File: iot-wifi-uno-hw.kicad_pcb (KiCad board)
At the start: 2 copper layers, 68.6 x 53.3 mm, 83 parts, among them CON1 BARREL_JACK, P1 CONN_01X08, P2 CONN_01X08, P3 CONN_01X06, P4 CONN_01X10, P5 CONN_01X04, Q1 Q_NPN_BEC, Q2 Q_NPN_BEC, U1 usb_mini_b, U2 MCP16311-MNY, U3 CH340G, U4 ESP-12E, U5 MCP6001R, U6 BD00GA5WEFJ, U7 IRLM6402, X1 CRYSTAL_ABM3C

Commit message: Fix Via & update assets
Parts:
- removed REF** (x12): gnd_via, ESP8266:gnd_via
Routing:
- net GND: track 300.3 -> 313.6 mm, vias 7 -> 10
- net GPIO14: track 56.7 -> 50.4 mm
- net GPIO5: track 133.7 -> 128.7 mm
- net GPIO4: track 131.9 -> 134.6 mm
- net MOSI: track 40.4 -> 38.5 mm
- net REST: track 110.7 -> 112.5 mm
- net MISO: track 30.9 -> 31.9 mm
- net GPIO0: track 83.7 -> 84.7 mm
- net SCLK: track 39.8 -> 38.9 mm
- net GPIO10: track 38.2 -> 37.5 mm
- net Net-(GPIO1-Pad1): track 81.3 -> 81.9 mm
- net GPIO13: track 46.1 -> 46.7 mm
- net GPIO16: track 58.2 -> 58.8 mm
- net GPIO15: track 47.7 -> 47.2 mm
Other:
- rule trace_min: 0.2 -> 0.254

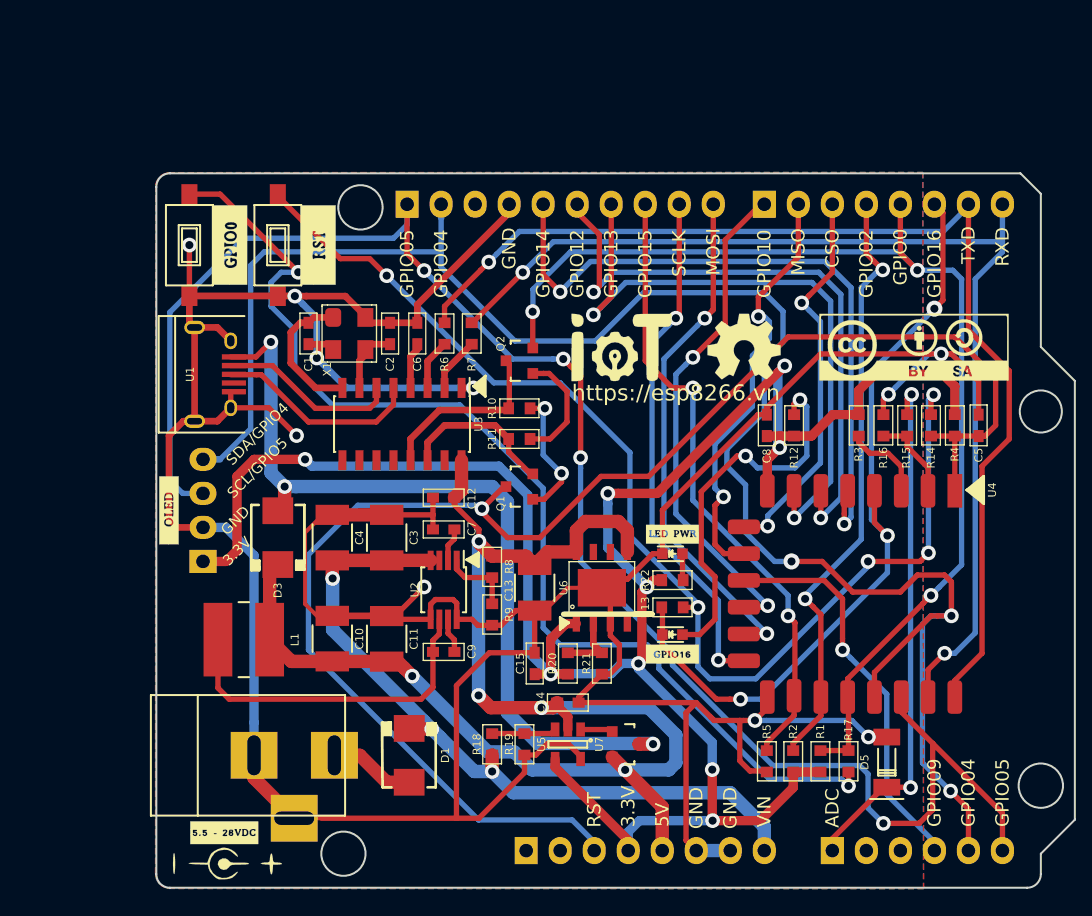
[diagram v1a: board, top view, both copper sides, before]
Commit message: change IC CH340G to PL2303HXD
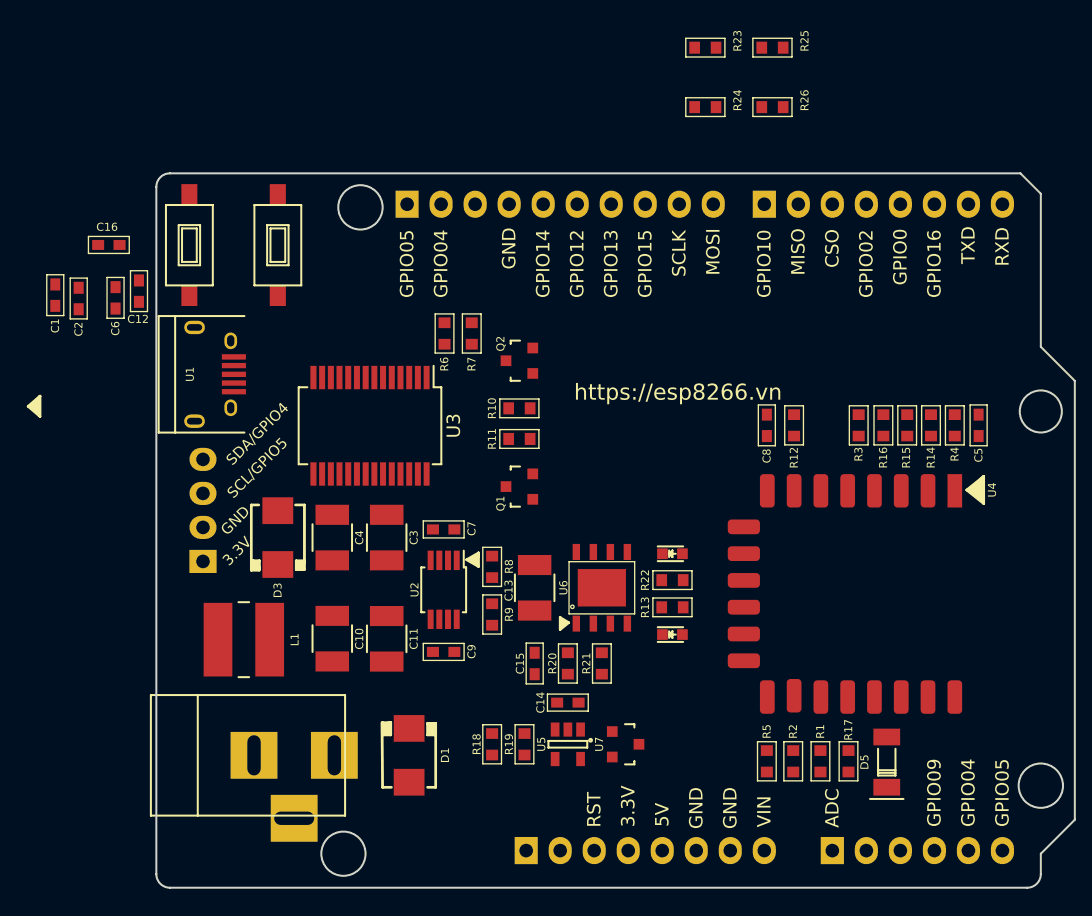
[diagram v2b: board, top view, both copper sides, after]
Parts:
- removed G***: LOGO, ESP8266:logo-jack-5528
- removed G***: LOGO, ESP8266:logo_openhardware_5x5mm
- removed G***: LOGO, ESP8266:logo-jack_7.4x3
- removed G***: LOGO, ESP8266:logo_cc-bby-sa_14.1x5mm
- removed G***: LOGO, ESP8266:logo-iotmakervn_7.5x5
- removed G***: LOGO, ESP8266:LEDPWR
- removed G***: LOGO, ESP8266:GPIO16
- removed G***: LOGO, ESP8266:RST
- removed G***: LOGO, ESP8266:GPIO0
- removed G***: LOGO, ESP8266:logo-iotmakervn_7
- removed X1: CRYSTAL_ABM3C, ESP8266:Crystal_SMD_3225_4Pads
- added C16: 10uF, ESP8266:C_0603, F.Cu at (106.0, 64.0)
- added R23: 4k7, ESP8266:R_0603, F.Cu at (150.5, 49.3)
- added R24: 27R, ESP8266:R_0603, F.Cu at (150.5, 53.7)
- added R25: 27R, ESP8266:R_0603, F.Cu at (155.5, 49.3)
- added R26: 1k5, ESP8266:R_0603, F.Cu at (155.5, 53.7)
- C1: value 22pF -> 0.1uF
- C12, C6: value 100nF -> 0.1uF
- C2: value 22pF -> 10uF
- R13: value 0R -> 0R-NC
- U3: value CH340G -> pl2303; footprint Housings_SOIC:SOIC-16_3.9x9.9mm_Pitch1.27mm -> Housings_SSOP:SSOP-28_5.3x10.2mm_Pitch0.65mm
- moved C12 27.5 mm to (108.2, 67.5), turned to 90 degrees
- moved C2 23.4 mm to (103.8, 68.0)
- moved C6 22.7 mm to (106.5, 68.0)
- moved C1 19.1 mm to (102.0, 67.8)
- moved U3 2.39 mm to (125.5, 77.5)
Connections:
- C1 pad 1: XO -> +3V3
- C12 pad 1: +5V -> GND
- C12 pad 2: GND -> +3V3
- C2 pad 1: XI -> VCC
- C6 pad 1: Net-(C6-Pad1) -> GND
- C6 pad 2: GND -> +5V
- Q1 pad 2: Net-(Q1-Pad2) -> RTS-N
- Q2 pad 3: Net-(Q2-Pad3) -> DTR-N
- R10 pad 1: Net-(Q2-Pad3) -> DTR-N
- R11 pad 1: Net-(Q1-Pad2) -> RTS-N
- R6 pad 2: Net-(R6-Pad2) -> RXD-2303
- R7 pad 2: Net-(R7-Pad2) -> TXD-2303
- U3 pad 1: GND -> TXD-2303
- U3 pad 10: (no net) -> DCD-N
- U3 pad 13: Net-(Q2-Pad3) -> (no net)
- U3 pad 14: Net-(Q1-Pad2) -> (no net)
- U3 pad 15: (no net) -> Net-(R24-Pad1)
- U3 pad 16: +5V -> Net-(R25-Pad1)
- U3 pad 2: Net-(R7-Pad2) -> DTR-N
- U3 pad 3: Net-(R6-Pad2) -> RTS-N
- U3 pad 4: Net-(C6-Pad1) -> +3V3
- U3 pad 5: D+ -> RXD-2303
- U3 pad 6: D- -> (no net)
- U3 pad 7: XI -> GND
- U3 pad 8: XO -> (no net)
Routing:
- net GND: track 313.6 -> 0.00 mm, vias 10 -> 0
- net +3V3: track 165.3 -> 0.00 mm, vias 9 -> 0
- net GPIO4: track 134.6 -> 0.00 mm, vias 3 -> 0
- net GPIO5: track 128.7 -> 0.00 mm, vias 4 -> 0
- net REST: track 112.5 -> 0.00 mm, vias 1 -> 0
- net +5V: track 105.5 -> 0.00 mm, vias 5 -> 0
- net Net-(R13-Pad2): track 88.8 -> 0.00 mm, vias 5 -> 0
- net GPIO0: track 84.7 -> 0.00 mm, vias 3 -> 0
- net TXD: track 82.6 -> 0.00 mm, vias 1 -> 0
- net Net-(GPIO1-Pad1): track 81.9 -> 0.00 mm, vias 2 -> 0
- net RXD: track 81.0 -> 0.00 mm, vias 2 -> 0
- net VCC: track 62.4 -> 0.00 mm, vias 3 -> 0
- net GPIO16: track 58.8 -> 0.00 mm, vias 3 -> 0
- net Vin: track 56.2 -> 0.00 mm, vias 3 -> 0
- net GPIO14: track 50.4 -> 0.00 mm, vias 2 -> 0
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- removed copper zone on B.Cu, net GND
- removed copper zone on F.Cu, net GND

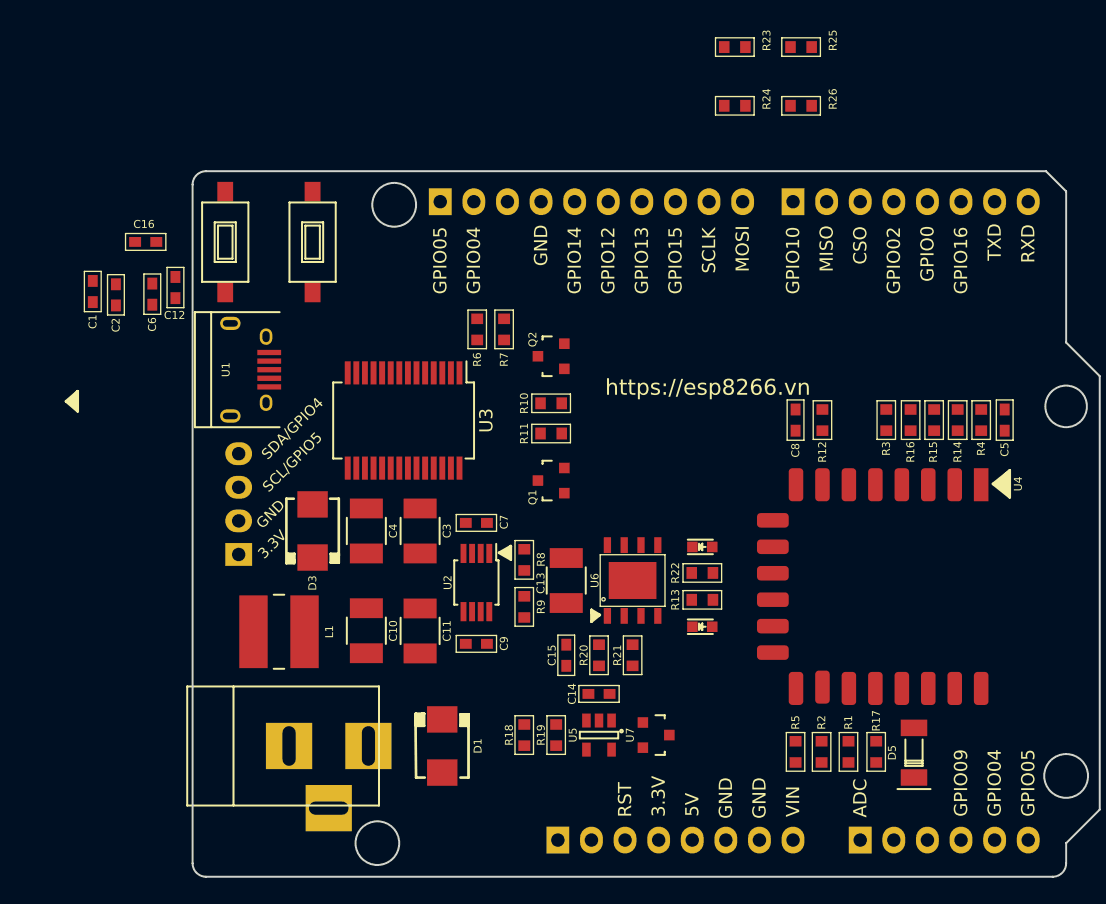
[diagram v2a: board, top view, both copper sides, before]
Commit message: setup new PCB
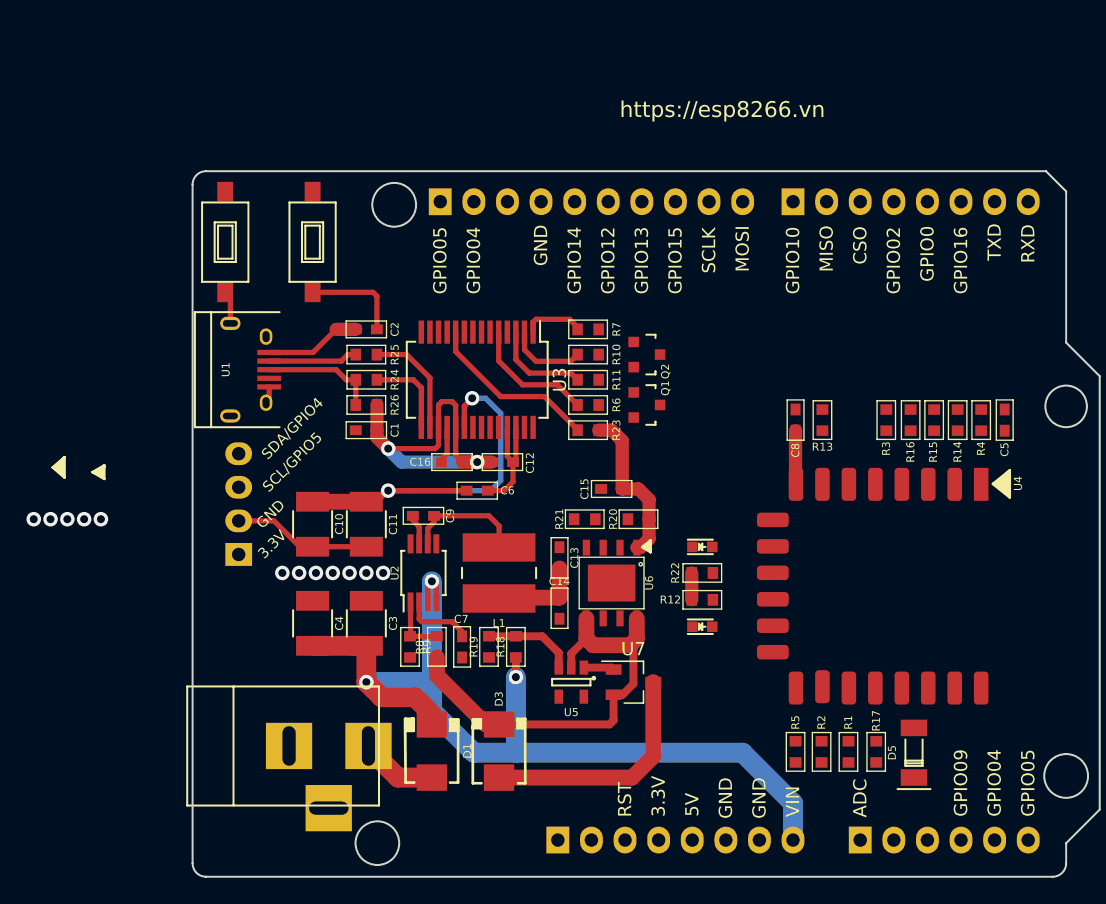
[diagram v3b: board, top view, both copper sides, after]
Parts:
- C13: footprint ESP8266:C_1210 -> ESP8266:C_0603
- U7: footprint TO_SOT_Packages_SMD:SOT-23 -> TO_SOT_Packages_SMD:SOT-23_Handsoldering
- moved R25 40.3 mm to (122.7, 72.5), turned to 180 degrees
- moved R26 39.9 mm to (122.7, 76.3)
- moved R24 34.7 mm to (122.7, 74.4), turned to 180 degrees
- moved R23 31.0 mm to (139.4, 78.2), turned to 180 degrees
- moved C6 28.7 mm to (131.1, 82.8), turned to 180 degrees
- moved C16 28.5 mm to (129.2, 80.6)
- moved C12 28.0 mm to (133.0, 80.6), turned to 180 degrees
- moved C1 23.2 mm to (122.7, 78.2), turned to 180 degrees
- moved D3 21.8 mm to (132.7, 102.5), turned to 270 degrees
- moved C2 19.1 mm to (122.7, 70.6), turned to 0 degrees
- moved L1 17.2 mm to (132.7, 89.0), turned to 270 degrees
- moved R12 16.3 mm to (148.1, 91.1), turned to 0 degrees
- moved R13 16.3 mm to (157.2, 77.5), turned to 90 degrees
- moved C15 13.0 mm to (141.2, 82.7), turned to 180 degrees
- moved R21 10.9 mm to (139.2, 85.0), turned to 180 degrees
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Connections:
- R26 pad 1: D- -> D+
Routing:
- net Vin: track 0.00 -> 71.9 mm, vias 0 -> 3
- net +5V: track 0.00 -> 70.9 mm, vias 0 -> 2
- net +3V3: track 0.00 -> 45.1 mm, vias 0 -> 2
- net GND: track 0.00 -> 33.7 mm
- net VCC: track 0.00 -> 25.2 mm
- net DCD-N: track 0.00 -> 13.2 mm
- net RXD-2303: track 0.00 -> 9.51 mm
- net Net-(C9-Pad2): track 0.00 -> 9.17 mm
- net D+: track 0.00 -> 8.77 mm
- net Net-(R25-Pad1): track 0.00 -> 8.48 mm
- net RTS-N: track 0.00 -> 7.37 mm
- net Net-(R18-Pad1): track 0.00 -> 6.91 mm
- net D-: track 0.00 -> 6.75 mm
- net Net-(R24-Pad1): track 0.00 -> 6.60 mm
- net DTR-N: track 0.00 -> 5.91 mm
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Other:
- net class Default: clearance 0.254 -> 0.2; trace_width 0.4 -> 0.6
- rule trace_clearance: 0.254 -> 0.2

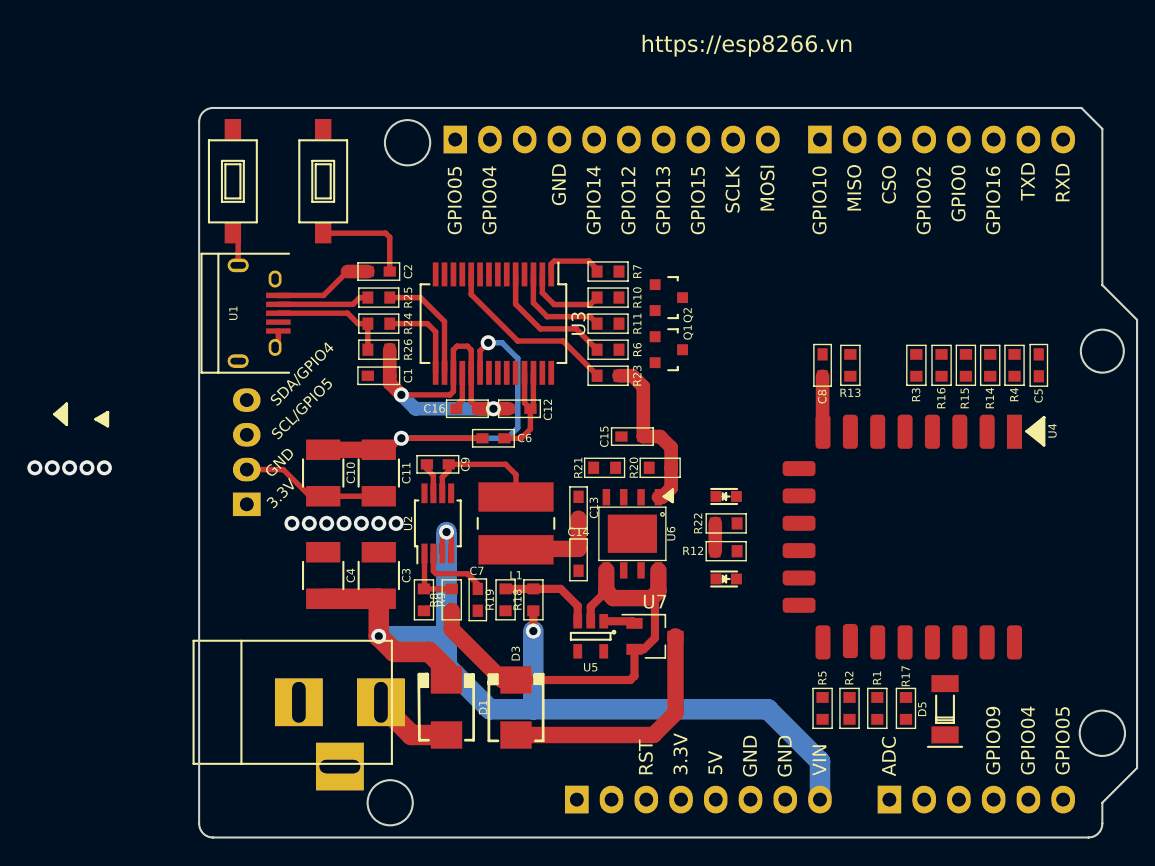
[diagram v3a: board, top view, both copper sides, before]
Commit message: fix error button & modify CH340G 5V to 3.3V, Update PCB
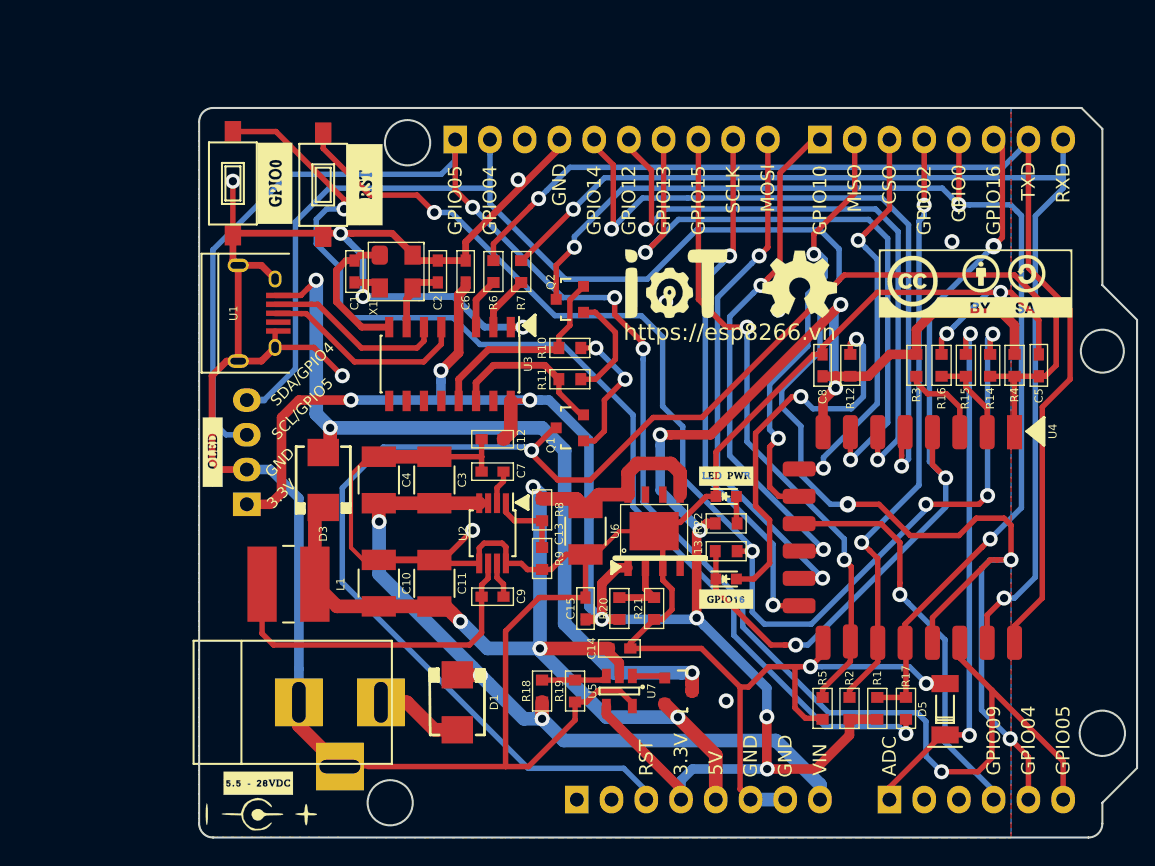
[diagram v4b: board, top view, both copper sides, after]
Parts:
- removed C16: 10uF, ESP8266:C_0603
- removed GPIO1: GPIO0, ESP8266:Tact_Switch_TS6X3.6
- removed R23: 4k7, ESP8266:R_0603
- removed R24, R25: 27R, ESP8266:R_0603
- removed R26: 1k5, ESP8266:R_0603
- removed RST1: REST, ESP8266:Tact_Switch_TS6X3.6
- added G***: LOGO, ESP8266:RST, F.Cu at (121.7, 64.3)
- added G***: LOGO, ESP8266:logo_cc-bby-sa_14.1x5mm, F.Cu at (166.3, 71.5)
- added G***: LOGO, ESP8266:GPIO0, F.Cu at (115.1, 64.2)
- added G***: LOGO, ESP8266:logo-iotmakervn_7, F.Cu at (110.5, 83.8)
- added G***: LOGO, ESP8266:logo-jack-5528, F.Cu at (113.9, 108.0)
- added G***: LOGO, ESP8266:logo-jack_7.4x3, F.Cu at (113.9, 110.2)
- added G***: LOGO, ESP8266:LEDPWR, F.Cu at (148.1, 85.6)
- added G***: LOGO, ESP8266:GPIO16, F.Cu at (148.1, 94.6)
- added G***: LOGO, ESP8266:logo-iotmakervn_7.5x5, F.Cu at (144.4, 71.5)
- added G***: LOGO, ESP8266:logo_openhardware_5x5mm, F.Cu at (153.4, 71.6)
- added SW1: RST, ESP8266:Tact_Switch_TS6X3.6, F.Cu at (118.6, 64.3)
- added SW2: GPIO0, ESP8266:Tact_Switch_TS6X3.6, F.Cu at (112.0, 64.2)
- added X1: CRYSTAL_ABM3C, ESP8266:Crystal_SMD_3225_4Pads, F.Cu at (124.0, 70.6)
- C1: value 0.1uF -> 22pF
- C12, C6: value 0.1uF -> 100nF
- C13: footprint ESP8266:C_0603 -> ESP8266:C_1210
- C2: value 10uF -> 22pF
- R13: value 0R-NC -> 0R
- U3: value pl2303 -> CH340G; footprint Housings_SSOP:SSOP-28_5.3x10.2mm_Pitch0.65mm -> Housings_SOIC:SOIC-16_3.9x9.9mm_Pitch1.27mm
- U7: footprint TO_SOT_Packages_SMD:SOT-23_Handsoldering -> TO_SOT_Packages_SMD:SOT-23
- moved D3 21.8 mm to (118.6, 85.9), turned to 90 degrees
- moved L1 17.2 mm to (116.1, 93.5), turned to 0 degrees
- moved R12 16.3 mm to (157.2, 77.5), turned to 90 degrees
- moved R13 16.3 mm to (148.1, 91.1), turned to 0 degrees
- moved C15 13.0 mm to (137.8, 95.2), turned to 90 degrees
- moved C6 12.4 mm to (129.0, 70.6), turned to 90 degrees
- moved R21 10.9 mm to (142.8, 95.2), turned to 270 degrees
- moved R20 10.7 mm to (140.3, 95.2), turned to 90 degrees
- moved C9 10.5 mm to (131.0, 94.4), turned to 180 degrees
- moved R6 10.1 mm to (131.1, 70.6), turned to 270 degrees
- moved C7 9.43 mm to (131.0, 85.2), turned to 180 degrees
- moved R8 9.32 mm to (134.6, 88.0), turned to 270 degrees
- moved Q1 9.22 mm to (136.7, 82.0), turned to 90 degrees
- moved R9 9.15 mm to (134.6, 91.6)
- moved C11 9.03 mm to (126.7, 93.4), turned to 90 degrees
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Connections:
- C1 pad 1: +3V3 -> XO
- C12 pad 1: GND -> +3V3
- C12 pad 2: +3V3 -> GND
- C2 pad 1: VCC -> XI
- C6 pad 1: GND -> +3V3
- C6 pad 2: +5V -> GND
- P2 pad 1: (no net) -> Net-(P2-Pad1)
- P2 pad 2: (no net) -> Net-(P2-Pad2)
- P3 pad 2: (no net) -> Net-(P3-Pad2)
- P3 pad 3: (no net) -> Net-(P3-Pad3)
- P4 pad 3: (no net) -> Net-(P4-Pad3)
- Q1 pad 2: RTS-N -> Net-(Q1-Pad2)
- Q2 pad 2: GPIO0 -> Net-(Q2-Pad2)
- Q2 pad 3: DTR-N -> GPIO0
- R10 pad 1: DTR-N -> Net-(Q2-Pad2)
- R11 pad 1: RTS-N -> Net-(Q1-Pad2)
- R6 pad 2: RXD-2303 -> Net-(R6-Pad2)
- R7 pad 2: TXD-2303 -> Net-(R7-Pad2)
- U1 pad 4: (no net) -> Net-(U1-Pad4)
- U3 pad 1: TXD-2303 -> GND
- U3 pad 10: DCD-N -> Net-(U3-Pad10)
- U3 pad 11: (no net) -> Net-(U3-Pad11)
- U3 pad 12: (no net) -> Net-(U3-Pad12)
- U3 pad 13: (no net) -> Net-(Q2-Pad2)
- U3 pad 14: (no net) -> Net-(Q1-Pad2)
- U3 pad 16: Net-(R25-Pad1) -> +3V3
- U3 pad 2: DTR-N -> Net-(R7-Pad2)
- U3 pad 3: RTS-N -> Net-(R6-Pad2)
- U3 pad 5: RXD-2303 -> D+
- U3 pad 6: (no net) -> D-
- U3 pad 7: GND -> XI
- U3 pad 8: (no net) -> XO
- U3 pad 9: (no net) -> Net-(U3-Pad9)
- U6 pad 4: (no net) -> Net-(U6-Pad4)
- U6 pad 6: (no net) -> Net-(U6-Pad6)
- U6 pad 7: (no net) -> Net-(U6-Pad7)
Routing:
- net GND: track 33.7 -> 311.7 mm, vias 0 -> 15
- net +3V3: track 45.1 -> 179.2 mm, vias 2 -> 11
- net GPIO4: track 0.00 -> 133.8 mm, vias 0 -> 3
- net GPIO5: track 0.00 -> 128.7 mm, vias 0 -> 4
- net REST: track 0.00 -> 114.1 mm, vias 0 -> 1
- net Net-(R13-Pad2): track 0.00 -> 90.8 mm, vias 0 -> 5
- net GPIO0: track 0.00 -> 85.8 mm, vias 0 -> 3
- net TXD: track 0.00 -> 82.6 mm, vias 0 -> 1
- net RXD: track 0.00 -> 81.0 mm, vias 0 -> 2
- net Net-(R17-Pad2): track 0.00 -> 80.8 mm, vias 0 -> 2
- net GPIO16: track 0.00 -> 58.4 mm, vias 0 -> 3
- net GPIO14: track 0.00 -> 50.5 mm, vias 0 -> 2
- net GPIO15: track 0.00 -> 47.2 mm, vias 0 -> 2
- net GPIO13: track 0.00 -> 46.7 mm, vias 0 -> 2
- net GPIO12: track 0.00 -> 45.8 mm, vias 0 -> 2
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- added copper zone on B.Cu, net GND
- added copper zone on F.Cu, net GND
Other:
- net class Default: clearance 0.2 -> 0.254; trace_width 0.6 -> 0.4
- rule trace_clearance: 0.2 -> 0.254
